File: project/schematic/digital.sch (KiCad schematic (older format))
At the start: 4 parts

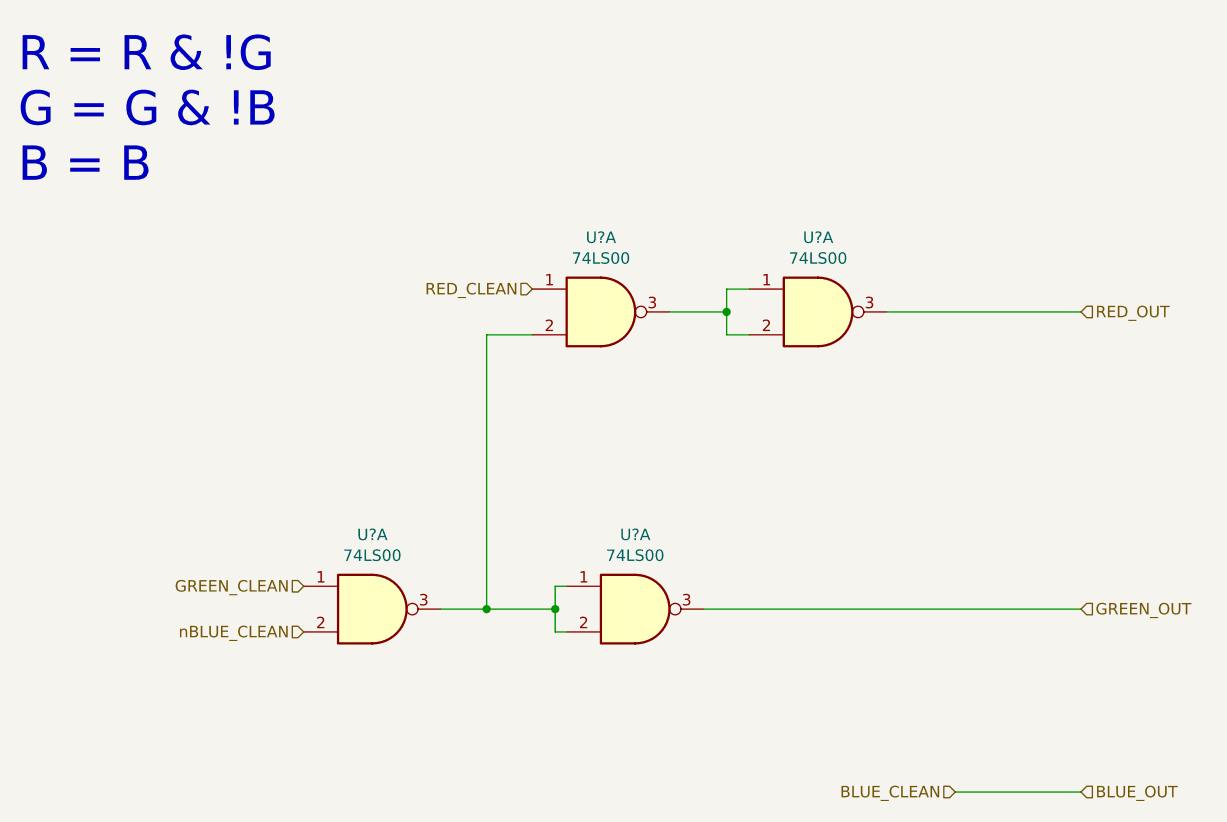
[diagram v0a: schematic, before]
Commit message: switch to high pass filters
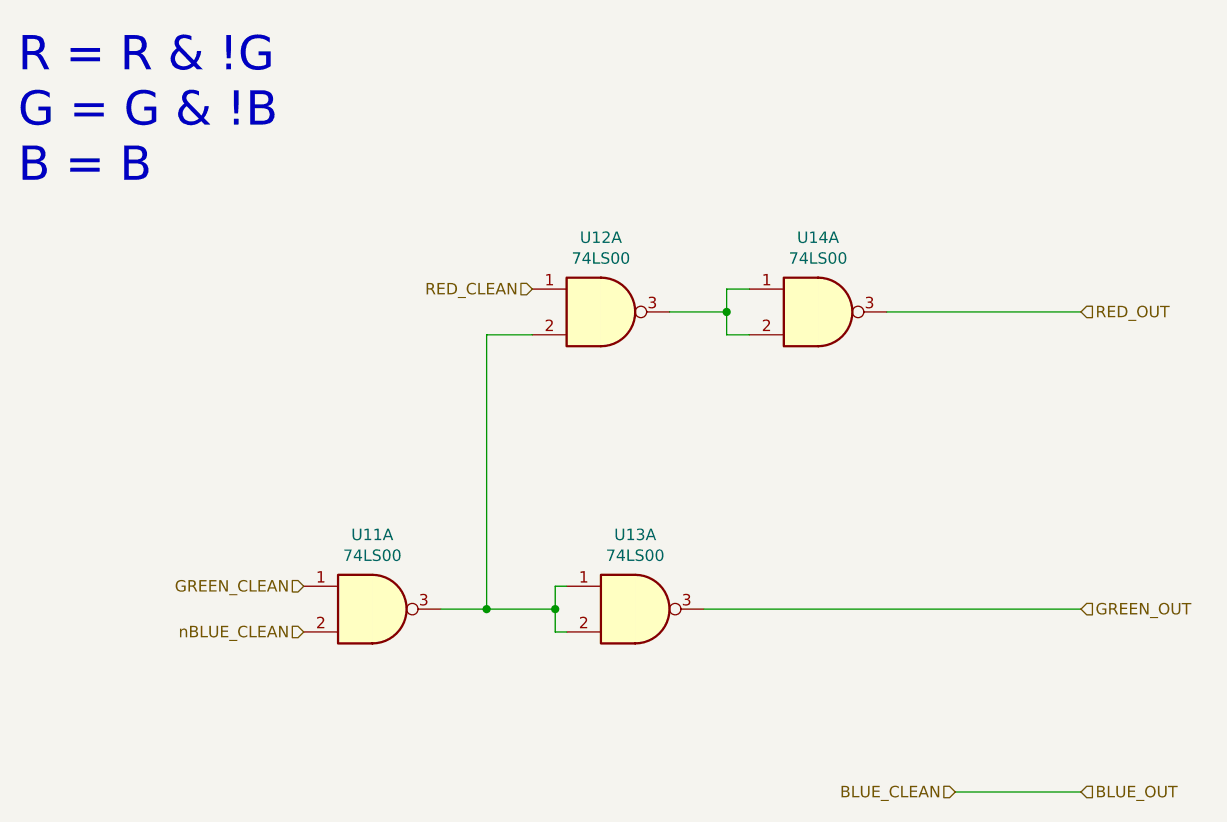
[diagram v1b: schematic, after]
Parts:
- gave numbers to parts that had none: 4
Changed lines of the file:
@@
 EESchema Schematic File Version 4
+LIBS:final_project_schematic-cache
 EELAYER 30 0
 EELAYER END
@@
 P 5000 4350
 AR Path="/5E4B9683" Ref="U?"  Part="1"
-AR Path="/5E4B412B/5E4B9683" Ref="U?"  Part="1"
-F 0 "U?" H 5000 4675 50  0000 C CNN
+AR Path="/5E4B412B/5E4B9683" Ref="U13"  Part="1"
+F 0 "U13" H 5000 4675 50  0000 C CNN
 F 1 "74LS00" H 5000 4584 50  0000 C CNN
 F 2 "" H 5000 4350 50  0001 C CNN
@@
 P 5800 3050
 AR Path="/5E4B9695" Ref="U?"  Part="1"
-AR Path="/5E4B412B/5E4B9695" Ref="U?"  Part="1"
-F 0 "U?" H 5800 3375 50  0000 C CNN
+AR Path="/5E4B412B/5E4B9695" Ref="U14"  Part="1"
+F 0 "U14" H 5800 3375 50  0000 C CNN
 F 1 "74LS00" H 5800 3284 50  0000 C CNN
 F 2 "" H 5800 3050 50  0001 C CNN
@@
 P 4850 3050
 AR Path="/5E4B969C" Ref="U?"  Part="1"
-AR Path="/5E4B412B/5E4B969C" Ref="U?"  Part="1"
-F 0 "U?" H 4850 3375 50  0000 C CNN
+AR Path="/5E4B412B/5E4B969C" Ref="U12"  Part="1"
+F 0 "U12" H 4850 3375 50  0000 C CNN
 F 1 "74LS00" H 4850 3284 50  0000 C CNN
 F 2 "" H 4850 3050 50  0001 C CNN
@@
 P 3850 4350
 AR Path="/5E4B96A3" Ref="U?"  Part="1"
-AR Path="/5E4B412B/5E4B96A3" Ref="U?"  Part="1"
-F 0 "U?" H 3850 4675 50  0000 C CNN
+AR Path="/5E4B412B/5E4B96A3" Ref="U11"  Part="1"
+F 0 "U11" H 3850 4675 50  0000 C CNN
 F 1 "74LS00" H 3850 4584 50  0000 C CNN
 F 2 "" H 3850 4350 50  0001 C CNN
